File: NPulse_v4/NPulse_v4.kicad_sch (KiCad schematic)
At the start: 50 parts, among them IC1 TXU0202QDCUR, J2 Conn_01x04_Pin, J3 Conn_01x06_Pin, J4 Conn_01x04_Pin, Q1 PMOS, Q2 NMOS, SW1 SW_Push, SW2 SW_SPDT, U1 STM32G484METx, Y1 16MHz

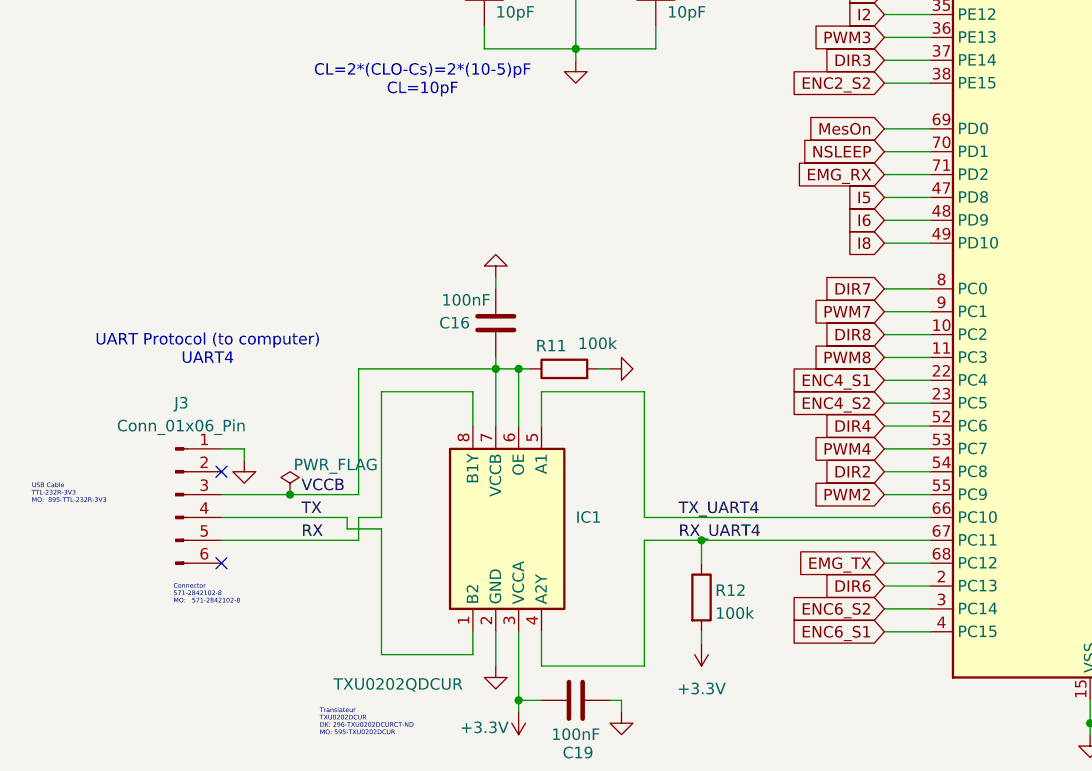
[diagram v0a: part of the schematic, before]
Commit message: Replace vias and change connectors footprint on control board
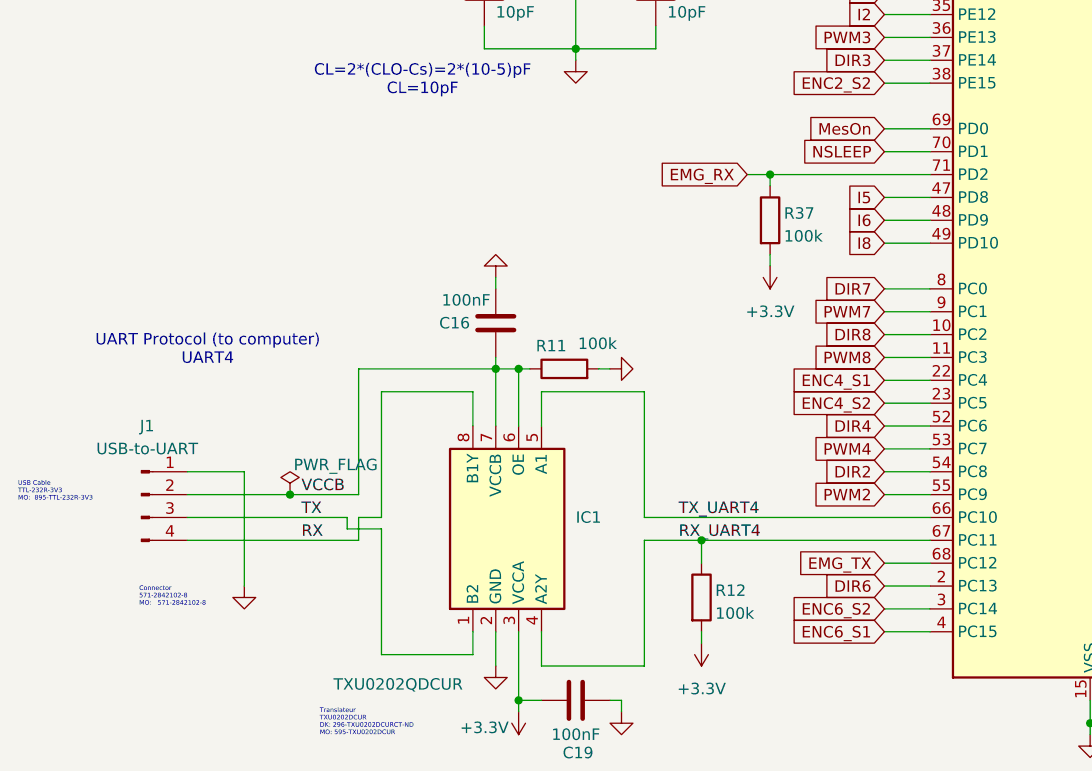
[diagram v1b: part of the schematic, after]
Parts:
- removed J3: Conn_01x06_Pin, Connector_PinHeader_2.54mm:PinHeader_1x06_P2.54mm_Vertical, symbol Connector:Conn_01x06_Pin
- added J1: USB-to-UART, Connector_PinHeader_2.54mm:PinHeader_1x04_P2.54mm_Vertical, symbol Connector:Conn_01x04_Pin
- added R37: 100k, Resistor_SMD:R_0402_1005Metric, symbol Device:R
- J2, J4: footprint Connector_PinHeader_2.00mm:PinHeader_1x04_P2.00mm_Vertical -> Connector_PinHeader_2.54mm:PinHeader_1x04_P2.54mm_Vertical
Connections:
- net +3.3V: now also R37.2
- net EMG_RX: now also R37.1
- net GND: now also J1.1 (Pin_1)
- net RX: now also J1.4 (Pin_4)
- net TX: now also J1.3 (Pin_3)
- net VCCB: now also J1.2 (Pin_2)
- no-connect marks 5 -> 3
